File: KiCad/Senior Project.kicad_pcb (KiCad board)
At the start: 4 copper layers, 54.3 x 70.8 mm, 68 parts, among them J1 USB_C_Receptacle_USB2.0_16P, J2 Screw_Terminal_01x02, J3 Screw_Terminal_01x06, Q2 IRLML0030, Q3 IRLML0030, Q4 IRLML0030, SW1 SW_Push, SW2 SW_Push, U1 ESP32-S3FH4R2, U2 TPS62162DSG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

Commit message: Added power plane
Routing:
- added copper zone on In1.Cu, net +3V3
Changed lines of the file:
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@@
 		(net 24)
+	)
+	(zone
+		(net 3)
+		(net_name "+3V3")
+		(layer "In1.Cu")
+		(hatch edge 0.5)
+		(connect_pads
+			(clearance 0.5)
+		)
+		(min_thickness 0.25)
+		(filled_areas_thickness no)
+		(fill yes
+			(thermal_gap 0.5)
+			(thermal_bridge_width 0.5)
+		)
+		(polygon
+			(pts
+				(xy 134.3 42.5) (xy 134.5 123.5) (xy 200 123.4) (xy 199.1 42.2) (xy 199 41.9)
+			)
+		)
 	)
 	(embedded_fonts no)

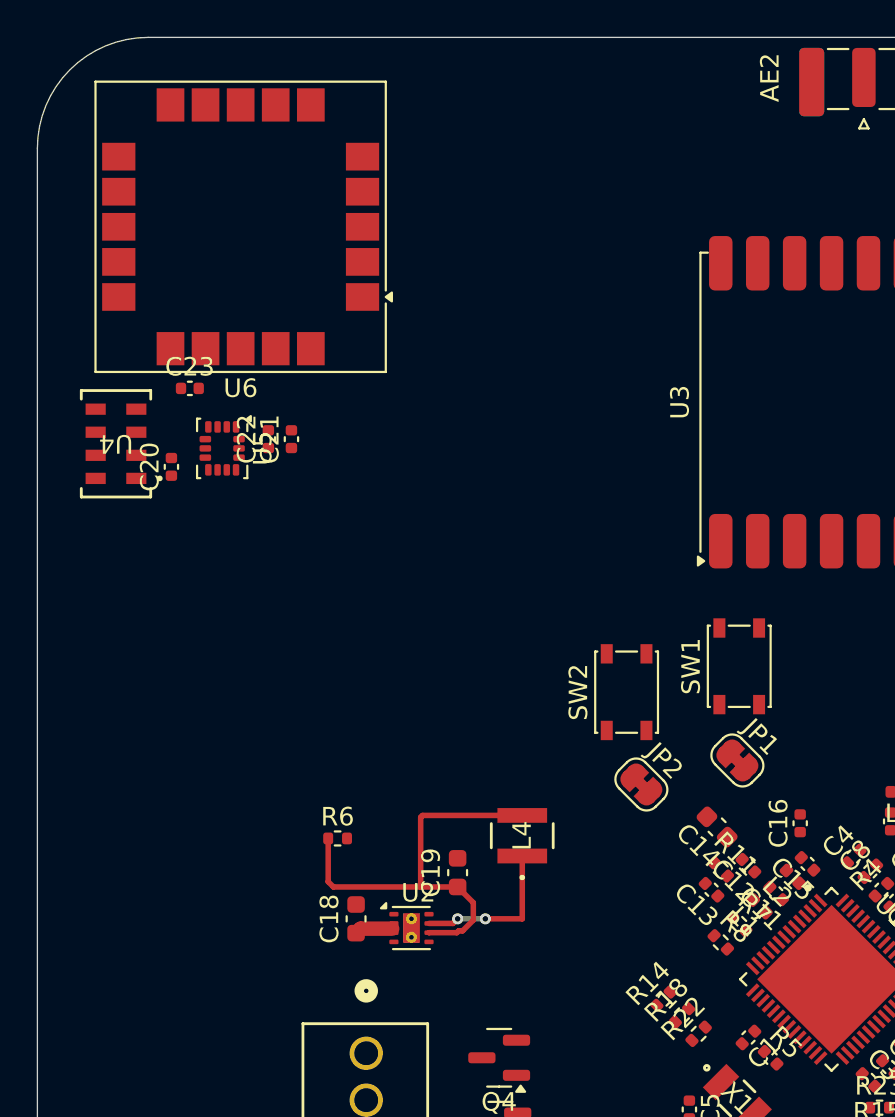
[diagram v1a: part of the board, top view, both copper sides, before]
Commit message: Added ground plane
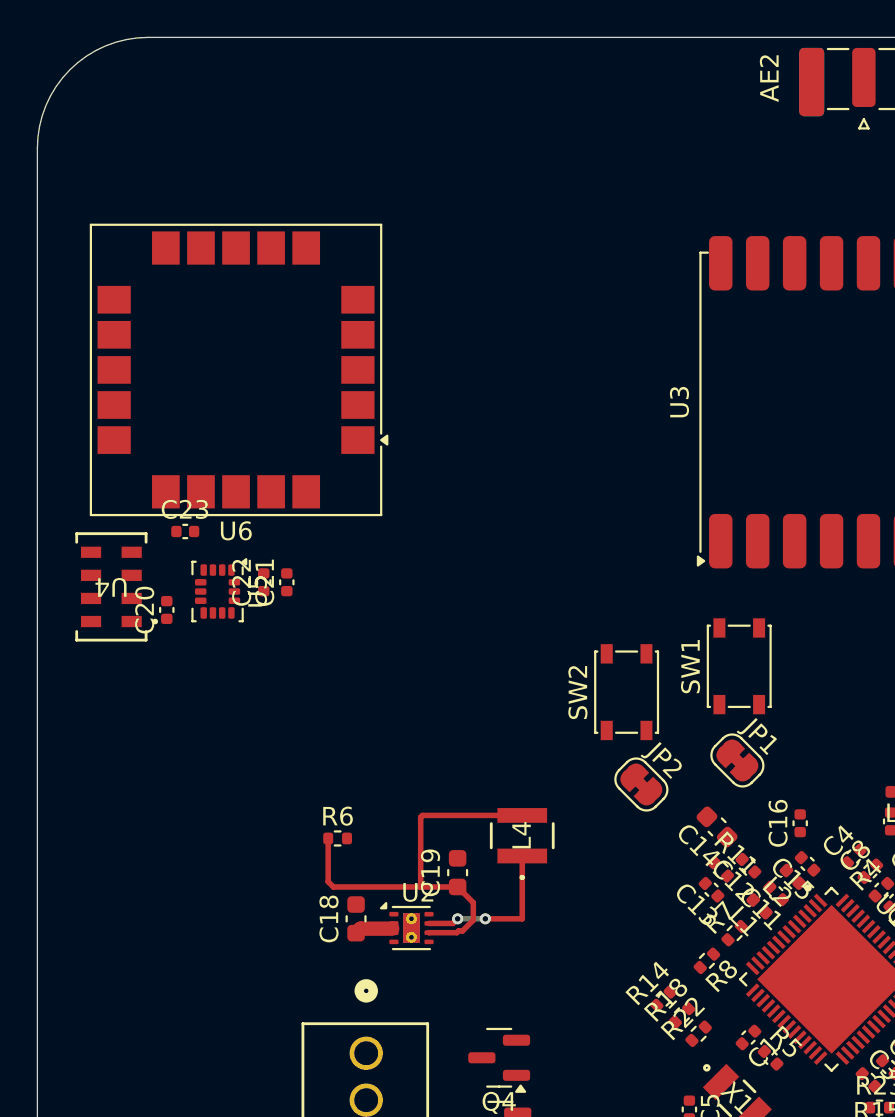
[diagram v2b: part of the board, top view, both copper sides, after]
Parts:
- moved C20 7.75 mm to (146.5, 80.2)
- moved C21 7.75 mm to (153.0, 78.8)
- moved C22 7.75 mm to (151.8, 78.8)
- moved C23 7.75 mm to (147.5, 76.0)
- moved U4 7.75 mm to (143.5, 79.0)
- moved U5 7.75 mm to (149.2, 79.2)
- moved U6 7.75 mm to (150.2, 67.2)
- moved R8 1.25 mm to (175.8, 99.2), turned to -135 degrees
- moved R7 0.56 mm to (177.2, 97.8), turned to 45 degrees
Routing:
- added copper zone on In2.Cu, net GND
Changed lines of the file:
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@@
 	(layers
 		(0 "F.Cu" signal)
-		(4 "In1.Cu" signal)
-		(6 "In2.Cu" signal)
+		(4 "In1.Cu" power)
+		(6 "In2.Cu" power)
 		(2 "B.Cu" signal)
 		(9 "F.Adhes" user "F.Adhesive")
@@
 	(footprint "Capacitor_SMD:C_0402_1005Metric"
 		(layer "F.Cu")
-		(at 147.75 68.25)
+		(at 147.5 76)
 		(descr "Capacitor SMD 0402 (1005 Metric), square (rectangular) end terminal, IPC_7351 nominal, (Body size source: IPC-SM-782 page 76, https://www.pcb-3d.com/wordpress/wp-content/uploads/ipc-sm-782a_amendment_1_and_2.pdf), generated with kicad-footprint-generator")
 		(tags "capacitor")
@@
 	(footprint "Package_LGA:LGA-14_3x2.5mm_P0.5mm_LayoutBorder3x4y"
 		(layer "F.Cu")
-		(at 149.5 71.5 -90)
+		(at 149.25 79.25 -90)
 		(descr "LGA, 14 Pin (https://www.st.com/resource/en/datasheet/lsm6ds3tr-c.pdf), generated with kicad-footprint-generator ipc_noLead_generator.py")
 		(tags "LGA NoLead")
@@
 	(footprint "Resistor_SMD:R_0402_1005Metric"
 		(layer "F.Cu")
-		(at 176.5 98.25 -45)
+		(at 175.75 99.25 -135)
 		(descr "Resistor SMD 0402 (1005 Metric), square (rectangular) end terminal, IPC_7351 nominal, (Body size source: IPC-SM-782 page 72, https://www.pcb-3d.com/wordpress/wp-content/uploads/ipc-sm-782a_amendment_1_and_2.pdf), generated with kicad-footprint-generator")
 		(tags "resistor")
 		(property "Reference" "R8"
-			(at 0 -1.17 135)
+			(at 0 -1.17 45)
 			(layer "F.SilkS")
 			(effects
@@
 		)
 		(property "Value" "10k"
-			(at 0 1.17 135)
+			(at 0 1.17 45)
 			(layer "F.Fab")
 			(effects
@@
 		)
 		(property "Datasheet" ""
-			(at 0 0 315)
+			(at 0 0 225)
 			(unlocked yes)
 			(layer "F.Fab")
@@
 		)
 		(property "Description" "Resistor, small symbol"
-			(at 0 0 315)
+			(at 0 0 225)
 			(unlocked yes)
 			(layer "F.Fab")
@@
 		)
 		(fp_line
-			(start -0.93 0.47)
-			(end -0.93 -0.47)
+			(start 0.93 0.47)
+			(end -0.93 0.47)
 			(stroke
 				(width 0.05)
@@
 		)
 		(fp_line
-			(start -0.93 -0.47)
-			(end 0.93 -0.47)
+			(start 0.93 -0.47)
+			(end 0.93 0.47)
 			(stroke
 				(width 0.05)
@@
 		)
 		(fp_line
-			(start 0.93 0.47)
-			(end -0.93 0.47)
+			(start -0.93 0.47)
+			(end -0.93 -0.47)
 			(stroke
 				(width 0.05)
@@
 		)
 		(fp_line
-			(start 0.93 -0.47)
-			(end 0.93 0.47)
+			(start -0.93 -0.47)
+			(end 0.93 -0.47)
 			(stroke
 				(width 0.05)
@@
 		)
 		(fp_line
-			(start -0.525 0.27)
-			(end -0.525 -0.27)
+			(start 0.525 0.27)
+			(end -0.525 0.27)
 			(stroke
 				(width 0.1)
@@
 		)
 		(fp_line
-			(start -0.525 -0.27)
-			(end 0.525 -0.27)
+			(start 0.525 -0.27)
+			(end 0.525 0.27)
 			(stroke
 				(width 0.1)
@@
 		)
 		(fp_line
-			(start 0.525 0.27)
-			(end -0.525 0.27)
+			(start -0.525 0.27)
+			(end -0.525 -0.27)
 			(stroke
 				(width 0.1)
@@
 		)
 		(fp_line
-			(start 0.525 -0.27)
-			(end 0.525 0.27)
+			(start -0.525 -0.27)
+			(end 0.525 -0.27)
 			(stroke
 				(width 0.1)
@@
 		)
 		(fp_text user "${REFERENCE}"
-			(at 0 0 135)
+			(at 0 0 45)
 			(layer "F.Fab")
 			(effects
@@
 		)
 		(pad "1" smd roundrect
-			(at -0.509999 0 315)
+			(at -0.509999 0 225)
 			(size 0.54 0.64)
 			(layers "F.Cu" "F.Mask" "F.Paste")
@@
 		)
 		(pad "2" smd roundrect
-			(at 0.509999 0 315)
+			(at 0.509999 0 225)
 			(size 0.54 0.64)
 			(layers "F.Cu" "F.Mask" "F.Paste")
@@
 	(footprint "Resistor_SMD:R_0402_1005Metric"
 		(layer "F.Cu")
-		(at 177.5 97.25 -45)
+		(at 177.25 97.75 45)
 		(descr "Resistor SMD 0402 (1005 Metric), square (rectangular) end terminal, IPC_7351 nominal, (Body size source: IPC-SM-782 page 72, https://www.pcb-3d.com/wordpress/wp-content/uploads/ipc-sm-782a_amendment_1_and_2.pdf), generated with kicad-footprint-generator")
 		(tags "resistor")
 		(property "Reference" "R7"
-			(at 0 -1.17 135)
+			(at 0 -1.17 45)
 			(layer "F.SilkS")
 			(effects
@@
 		)
 		(property "Value" "10k"
-			(at 0 1.17 135)
+			(at 0 1.17 45)
 			(layer "F.Fab")
 			(effects
@@
 		)
 		(property "Datasheet" ""
-			(at 0 0 315)
+			(at 0 0 45)
 			(unlocked yes)
 			(layer "F.Fab")
@@
 		)
 		(property "Description" "Resistor, small symbol"
-			(at 0 0 315)
+			(at 0 0 45)
 			(unlocked yes)
 			(layer "F.Fab")
@@
 		(attr smd)
 		(fp_line
-			(start -0.153641 0.38)
-			(end 0.153641 0.38)
+			(start -0.153641 -0.38)
+			(end 0.153641 -0.38)
 			(stroke
 				(width 0.12)
@@
 		)
 		(fp_line
-			(start -0.153641 -0.38)
-			(end 0.153641 -0.38)
+			(start -0.153641 0.38)
+			(end 0.153641 0.38)
 			(stroke
 				(width 0.12)
@@
 		)
 		(fp_line
-			(start -0.93 0.47)
-			(end -0.93 -0.47)
+			(start -0.93 -0.47)
+			(end 0.93 -0.47)
 			(stroke
 				(width 0.05)
@@
 		)
 		(fp_line
-			(start -0.93 -0.47)
-			(end 0.93 -0.47)
+			(start -0.93 0.47)
+			(end -0.93 -0.47)
 			(stroke
 				(width 0.05)
@@
 		)
 		(fp_line
-			(start 0.93 0.47)
-			(end -0.93 0.47)
+			(start 0.93 -0.47)
+			(end 0.93 0.47)
 			(stroke
 				(width 0.05)
@@
 		)
 		(fp_line
-			(start 0.93 -0.47)
-			(end 0.93 0.47)
+			(start 0.93 0.47)
+			(end -0.93 0.47)
 			(stroke
 				(width 0.05)
@@
 		)
 		(fp_line
-			(start -0.525 0.27)
-			(end -0.525 -0.27)
+			(start -0.525 -0.27)
+			(end 0.525 -0.27)
 			(stroke
 				(width 0.1)
@@
 		)
 		(fp_line
-			(start -0.525 -0.27)
-			(end 0.525 -0.27)
+			(start -0.525 0.27)
+			(end -0.525 -0.27)
 			(stroke
 				(width 0.1)
@@
 		)
 		(fp_line
-			(start 0.525 0.27)
-			(end -0.525 0.27)
+			(start 0.525 -0.27)
+			(end 0.525 0.27)
 			(stroke
 				(width 0.1)
@@
 		)
 		(fp_line
-			(start 0.525 -0.27)
-			(end 0.525 0.27)
+			(start 0.525 0.27)
+			(end -0.525 0.27)
 			(stroke
 				(width 0.1)
@@
 		)
 		(fp_text user "${REFERENCE}"
-			(at 0 0 135)
+			(at 0 0 45)
 			(layer "F.Fab")
 			(effects
@@
 		)
 		(pad "1" smd roundrect
-			(at -0.509999 0 315)
+			(at -0.509999 0 45)
 			(size 0.54 0.64)
 			(layers "F.Cu" "F.Mask" "F.Paste")
@@
 		)
 		(pad "2" smd roundrect
-			(at 0.509999 0 315)
+			(at 0.509999 0 45)
 			(size 0.54 0.64)
 			(layers "F.Cu" "F.Mask" "F.Paste")
@@
 	(footprint "Capacitor_SMD:C_0402_1005Metric"
 		(layer "F.Cu")
-		(at 152 71 90)
+		(at 151.75 78.75 90)
 		(descr "Capacitor SMD 0402 (1005 Metric), square (rectangular) end terminal, IPC_7351 nominal, (Body size source: IPC-SM-782 page 76, https://www.pcb-3d.com/wordpress/wp-content/uploads/ipc-sm-782a_amendment_1_and_2.pdf), generated with kicad-footprint-generator")
 		(tags "capacitor")
@@
 	(footprint "RF_GPS:ublox_SAM-M8Q"
 		(layer "F.Cu")
-		(at 150.5 59.5 180)
+		(at 150.25 67.25 180)
 		(descr "GPS Module, 15.5x15.5x6.3mm, https://www.u-blox.com/sites/default/files/SAM-M8Q_HardwareIntegrationManual_%28UBX-16018358%29.pdf")
 		(tags "ublox SAM-M8Q")
@@
 	(footprint "MS56:SON8_MS5611_TEC"
 		(layer "F.Cu")
-		(at 143.75 71.25 180)
+		(at 143.5 79 180)
 		(tags "MS560702BA03-50 ")
 		(property "Reference" "U4"
@@
 	(footprint "Capacitor_SMD:C_0402_1005Metric"
 		(layer "F.Cu")
-		(at 146.75 72.5 90)
+		(at 146.5 80.25 90)
 		(descr "Capacitor SMD 0402 (1005 Metric), square (rectangular) end terminal, IPC_7351 nominal, (Body size source: IPC-SM-782 page 76, https://www.pcb-3d.com/wordpress/wp-content/uploads/ipc-sm-782a_amendment_1_and_2.pdf), generated with kicad-footprint-generator")
 		(tags "capacitor")
@@
 	(footprint "Capacitor_SMD:C_0402_1005Metric"
 		(layer "F.Cu")
-		(at 153.25 71 90)
+		(at 153 78.75 90)
 		(descr "Capacitor SMD 0402 (1005 Metric), square (rectangular) end terminal, IPC_7351 nominal, (Body size source: IPC-SM-782 page 76, https://www.pcb-3d.com/wordpress/wp-content/uploads/ipc-sm-782a_amendment_1_and_2.pdf), generated with kicad-footprint-generator")
 		(tags "capacitor")
@@
 		(net 24)
 	)
+	(segment
+		(start 142.4 79.625)
+		(end 142.6029 79.625)
+		(width 0.2)
+		(layer "F.Cu")
+		(net 29)
+	)
 	(zone
 		(net 3)
@@
 			)
 		)
+	)
+	(zone
+		(net 2)
+		(net_name "GND")
+		(layer "In2.Cu")
+		(name "GND")
+		(hatch edge 0.5)
+		(priority 1)
+		(connect_pads
+			(clearance 0.5)
+		)
+		(min_thickness 0.25)
+		(filled_areas_thickness no)
+		(fill yes
+			(thermal_gap 0.5)
+			(thermal_bridge_width 0.5)
+		)
+		(polygon
+			(pts
+				(xy 132.75 126.25) (xy 200.75 126.25) (xy 199.75 39.5) (xy 132.5 40)
+			)
+		)

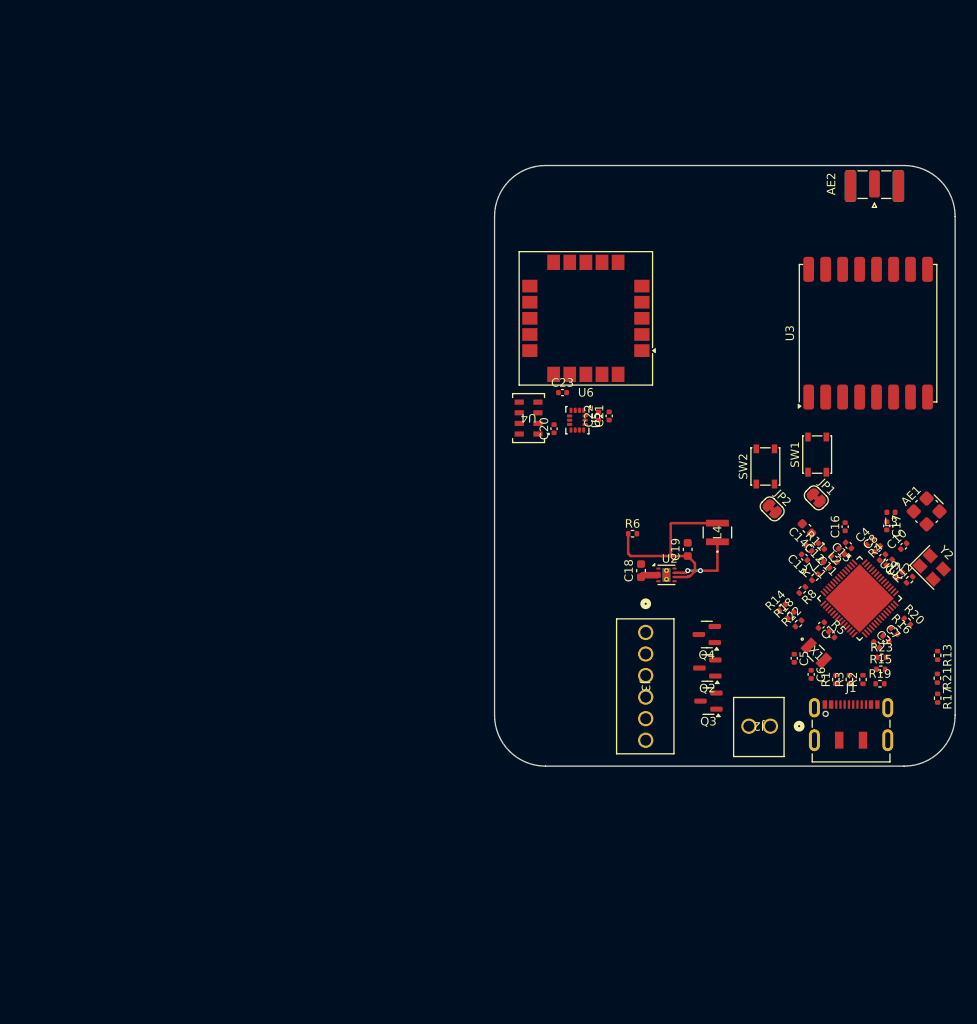
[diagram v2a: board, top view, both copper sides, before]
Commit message: GPS 1 cm space
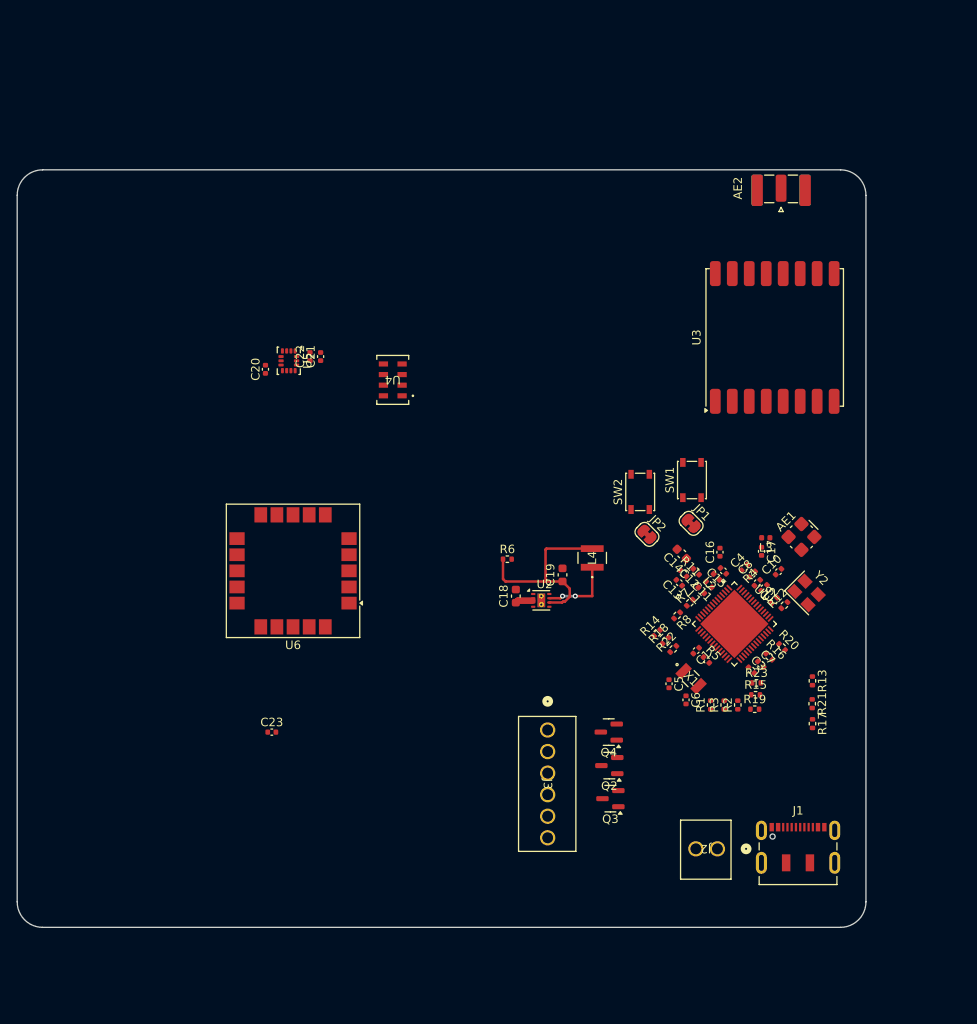
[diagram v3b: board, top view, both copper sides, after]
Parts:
- moved C23 52.7 mm to (113.2, 116.0)
- moved U6 45.6 mm to (115.8, 97.0)
- moved C20 34.7 mm to (112.5, 73.2)
- moved C21 34.7 mm to (119.0, 71.8)
- moved C22 34.7 mm to (117.8, 71.8)
- moved U5 34.7 mm to (115.2, 72.2)
- moved U4 16.6 mm to (127.5, 74.5)
- moved J3 16.3 mm to (145.8, 115.8)
- moved Q2 16.3 mm to (153.0, 119.9)
- moved Q3 16.3 mm to (153.1, 123.8)
- moved Q4 16.3 mm to (152.9, 116.0)
- moved J1 15.7 mm to (175.2, 130.2)
- moved J2 15.7 mm to (165.8, 129.8)
- moved AE1 15.1 mm to (175.7, 93.0)
- moved C1 15.1 mm to (163.2, 106.4)
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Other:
- board size 54.3 x 70.8 mm -> 100 x 89.2 mm

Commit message: Routing, placement
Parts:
- moved U6 60.7 mm to (167.5, 128.8), turned to 90 degrees
- moved C20 55.2 mm to (151.0, 112.8)
- moved J1 54.4 mm to (129.5, 100.9), turned to -90 degrees
- moved J2 52.4 mm to (130.0, 91.4), turned to 90 degrees
- moved C21 51.0 mm to (149.0, 113.0), turned to 180 degrees
- moved U5 50.7 mm to (148.2, 110.8), turned to 0 degrees
- moved J3 46.6 mm to (143.3, 69.3)
- moved Q2 46.6 mm to (150.6, 73.4)
- moved Q3 46.6 mm to (150.7, 77.3)
- moved Q4 46.6 mm to (150.5, 69.5)
- moved C22 46.4 mm to (146.6, 108.1), turned to 180 degrees
- moved U4 45.5 mm to (154.0, 111.5), turned to 0 degrees
- moved C23 45.3 mm to (157.5, 125.8), turned to -90 degrees
- moved C18 22.5 mm to (128.8, 118.1)
- moved C19 22.5 mm to (134.2, 115.6)
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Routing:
- net /SCL: track 0.00 -> 42.7 mm
- net /SDA: track 0.00 -> 35.8 mm, vias 0 -> 2
- net +3V3: track 23.6 -> 35.9 mm
- net GND: track 0.00 -> 9.86 mm
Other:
- board size 100 x 89.2 mm -> 59.2 x 89.2 mm
